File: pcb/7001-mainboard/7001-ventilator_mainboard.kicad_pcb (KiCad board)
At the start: 4 copper layers, 65 x 56.5 mm, 91 parts, among them J1 USB_B_Micro, J10 UART, J2 SWD, J3 Conn_01x02_MountingPin, J4 DNI, J5 24VIN, J6 5V out, J7 PREG_PWR, J8 PREG_SIGNALS, J9 Raspberry_Pi_2_3, Q1 IRLML6244TRPbF, U1 MPRLS0001PG0000SA, U10 ABPMAND001PG2A3, U11 MPVZ5010GW6U, U12 MPVZ5010GW6U, U2 TPD2E2U06, U3 LPC11U37FBD48-401_, U4 MCP1825S, U7 AD5410AREZ, U8 MPRLS0001PG0000SA, U9 ABPMAND001PG2A3, Y1 MCSJK-7U-12.00-10-10-80-B-10

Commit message: schematics: ready for review?
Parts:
- removed Q1: IRLML6244TRPbF, Package_TO_SOT_SMD:SOT-23
- removed TP10: valve_2_fet, TestPoint:TestPoint_Pad_D1.0mm
- added C11: 1uF, Capacitor_SMD:C_0805_2012Metric, F.Cu at (74.0, 218.4)
- added C16: 10uF, Capacitor_SMD:C_0805_2012Metric, F.Cu at (77.5, 215.1)
- added C38: 10uF 50V, Capacitor_SMD:C_1206_3216Metric, F.Cu at (35.8, 230.3)
- added C39: 100nF 50V, Capacitor_SMD:C_0805_2012Metric, F.Cu at (81.9, 206.8)
- added C40: 100nF, Capacitor_SMD:C_0805_2012Metric, F.Cu at (44.0, 233.4)
- added C41: 100nF 50V, Capacitor_SMD:C_0805_2012Metric, F.Cu at (39.6, 233.4)
- added C42: 10uF 50V, Capacitor_SMD:C_1206_3216Metric, F.Cu at (47.0, 230.3)
- added C43: 100nF, Capacitor_SMD:C_0805_2012Metric, F.Cu at (35.2, 233.4)
- added C44: 10uF 50V, Capacitor_SMD:C_1206_3216Metric, F.Cu at (69.0, 218.6)
- added C45: 2.2nF 50V, Capacitor_SMD:C_0805_2012Metric, F.Cu at (48.4, 233.4)
- added D2: D_Schottky, Diode_SMD:D_SOD-123F, F.Cu at (72.6, 215.3)
- added J11: I2C, Jitter_Footprints:TerminalBlock_Wurth_WR-TBL_691322110004_1x04_P3.50mm_Horizontal, F.Cu at (36.2, 208.2)
- added J12: FLOW_SENSORS, Jitter_Footprints:TerminalBlock_Wurth_WR-TBL_691322110003_1x03_P3.50mm_Horizontal, F.Cu at (36.2, 219.8)
- added J13: PREG_PWR, Jitter_Footprints:TerminalBlock_Wurth_WR-TBL_691322110002_1x02_P3.50mm_Horizontal, F.Cu at (49.6, 219.8)
- added J14: PREG_PWR, Jitter_Footprints:TerminalBlock_Wurth_WR-TBL_691322110002_1x02_P3.50mm_Horizontal, F.Cu at (63.1, 208.2)
- added R22: 0, Resistor_SMD:R_0805_2012Metric, F.Cu at (39.6, 245.4)
- added R23: 0, Resistor_SMD:R_0805_2012Metric, F.Cu at (44.0, 239.5)
- added R24: DNI, Resistor_SMD:R_0805_2012Metric, F.Cu at (39.6, 242.4)
- added R25: DNI, Resistor_SMD:R_0805_2012Metric, F.Cu at (35.2, 245.4)
- added R26: DNI, Resistor_SMD:R_0805_2012Metric, F.Cu at (39.6, 239.5)
- added R27: 0, Resistor_SMD:R_0805_2012Metric, F.Cu at (35.2, 242.4)
- added R28: 0, Resistor_SMD:R_0805_2012Metric, F.Cu at (35.2, 239.5)
- added R29: 1k5, Resistor_SMD:R_0805_2012Metric, F.Cu at (68.4, 224.7)
- added R30: DNI, Resistor_SMD:R_0805_2012Metric, F.Cu at (72.8, 221.8)
- added R31: 3.3k, Resistor_SMD:R_0805_2012Metric, F.Cu at (81.9, 212.8)
- added R32: 10k, Resistor_SMD:R_0805_2012Metric, F.Cu at (68.4, 227.7)
- added R33: 1k5, Resistor_SMD:R_0805_2012Metric, F.Cu at (78.5, 218.1)
- added R34: 4.7k, Resistor_SMD:R_0805_2012Metric, F.Cu at (72.8, 224.7)
- added R35: 1k5, Resistor_SMD:R_0805_2012Metric, F.Cu at (77.2, 221.4)
- added R36: 4.7k, Resistor_SMD:R_0805_2012Metric, F.Cu at (68.4, 230.6)
- added U13: ITS4142NHUMA1, Package_TO_SOT_SMD:SOT-223, F.Cu at (74.8, 209.5)
- added U14: ITS4142NHUMA1, Package_TO_SOT_SMD:SOT-223, F.Cu at (61.3, 229.4)
- added U6: LM2937IMP-12/NOPB, Package_TO_SOT_SMD:SOT-223-3_TabPin2, F.Cu at (61.3, 221.1)
- C17: value 2.2nF -> 2.2nF 50V
- C18: value 1uF -> 10uF 50V; footprint Capacitor_SMD:C_0805_2012Metric -> Capacitor_SMD:C_1206_3216Metric
- C19: value 2.2nF -> 100nF 50V
- D1: value BZT52C10+ -> D_Schottky; footprint Diode_SMD:D_SOD-123 -> Diode_SMD:D_SOD-123F
- J3: value Conn_01x02_MountingPin -> 12V; footprint Jitter_Footprints:JST_ZH_S2B-ZR-SM4A-TF_1x02-1MP_P1.5mm_Horizontal -> Jitter_Footprints:TerminalBlock_Wurth_WR-TBL_691322110002_1x02_P3.50mm_Horizontal
- R6: value 1k -> 68k
- R7: value 4.7k -> DNI
- U4: value MCP1825S -> MCP1825S-3302E
- moved C18 213.5 mm to (41.4, 230.3)
- moved R6 211.4 mm to (52.8, 233.4)
- moved D1 207.9 mm to (52.6, 230.3)
- moved R7 190.5 mm to (68.4, 221.8)
- moved J3 188.4 mm to (53.1, 208.2)
- moved C19 170.2 mm to (81.9, 209.8)
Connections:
- C17 pad 1: +6V -> /24V_SW1_OUT
- C18 pad 1: +6V -> +24V
- C19 pad 1: Net-(C19-Pad1) -> +24V
- D1 pad 1: Net-(C19-Pad1) -> /24V_SW1_OUT
- J10 pad 2: /UART_TX -> (no net)
- J10 pad 3: /UART_RX -> (no net)
- J3 pad 1: +6V -> GND
- J3 pad 2: Net-(C19-Pad1) -> +12V
- JP1 pad 1: (no net) -> /DCDC_5V
- R6 pad 2: /pwm_1 -> +24V
- R7 pad 1: GND -> Net-(R30-Pad2)
- R7 pad 2: /pwm_1 -> /DCDC_5V
- U1 pad 12: +3V3 -> Net-(R22-Pad2)
- U10 pad 2: +3V3 -> Net-(R23-Pad2)
- U10 pad 5: /I2C_SCL -> /pressure_sensor/P_SDA
- U10 pad 6: /I2C_SDA -> /pressure_sensor/P_SCL
- U3 pad 30: /pwm_1 -> (no net)
- U8 pad 12: +3V3 -> Net-(R23-Pad2)
- U9 pad 2: +3V3 -> Net-(R22-Pad2)
- U9 pad 5: /I2C_SCL -> /pressure_sensor/P_SDA
- U9 pad 6: /I2C_SDA -> /pressure_sensor/P_SCL
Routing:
- net Net-(R23-Pad2): track 0.00 -> 4.48 mm
- net +3V3: track 4.48 -> 0.00 mm

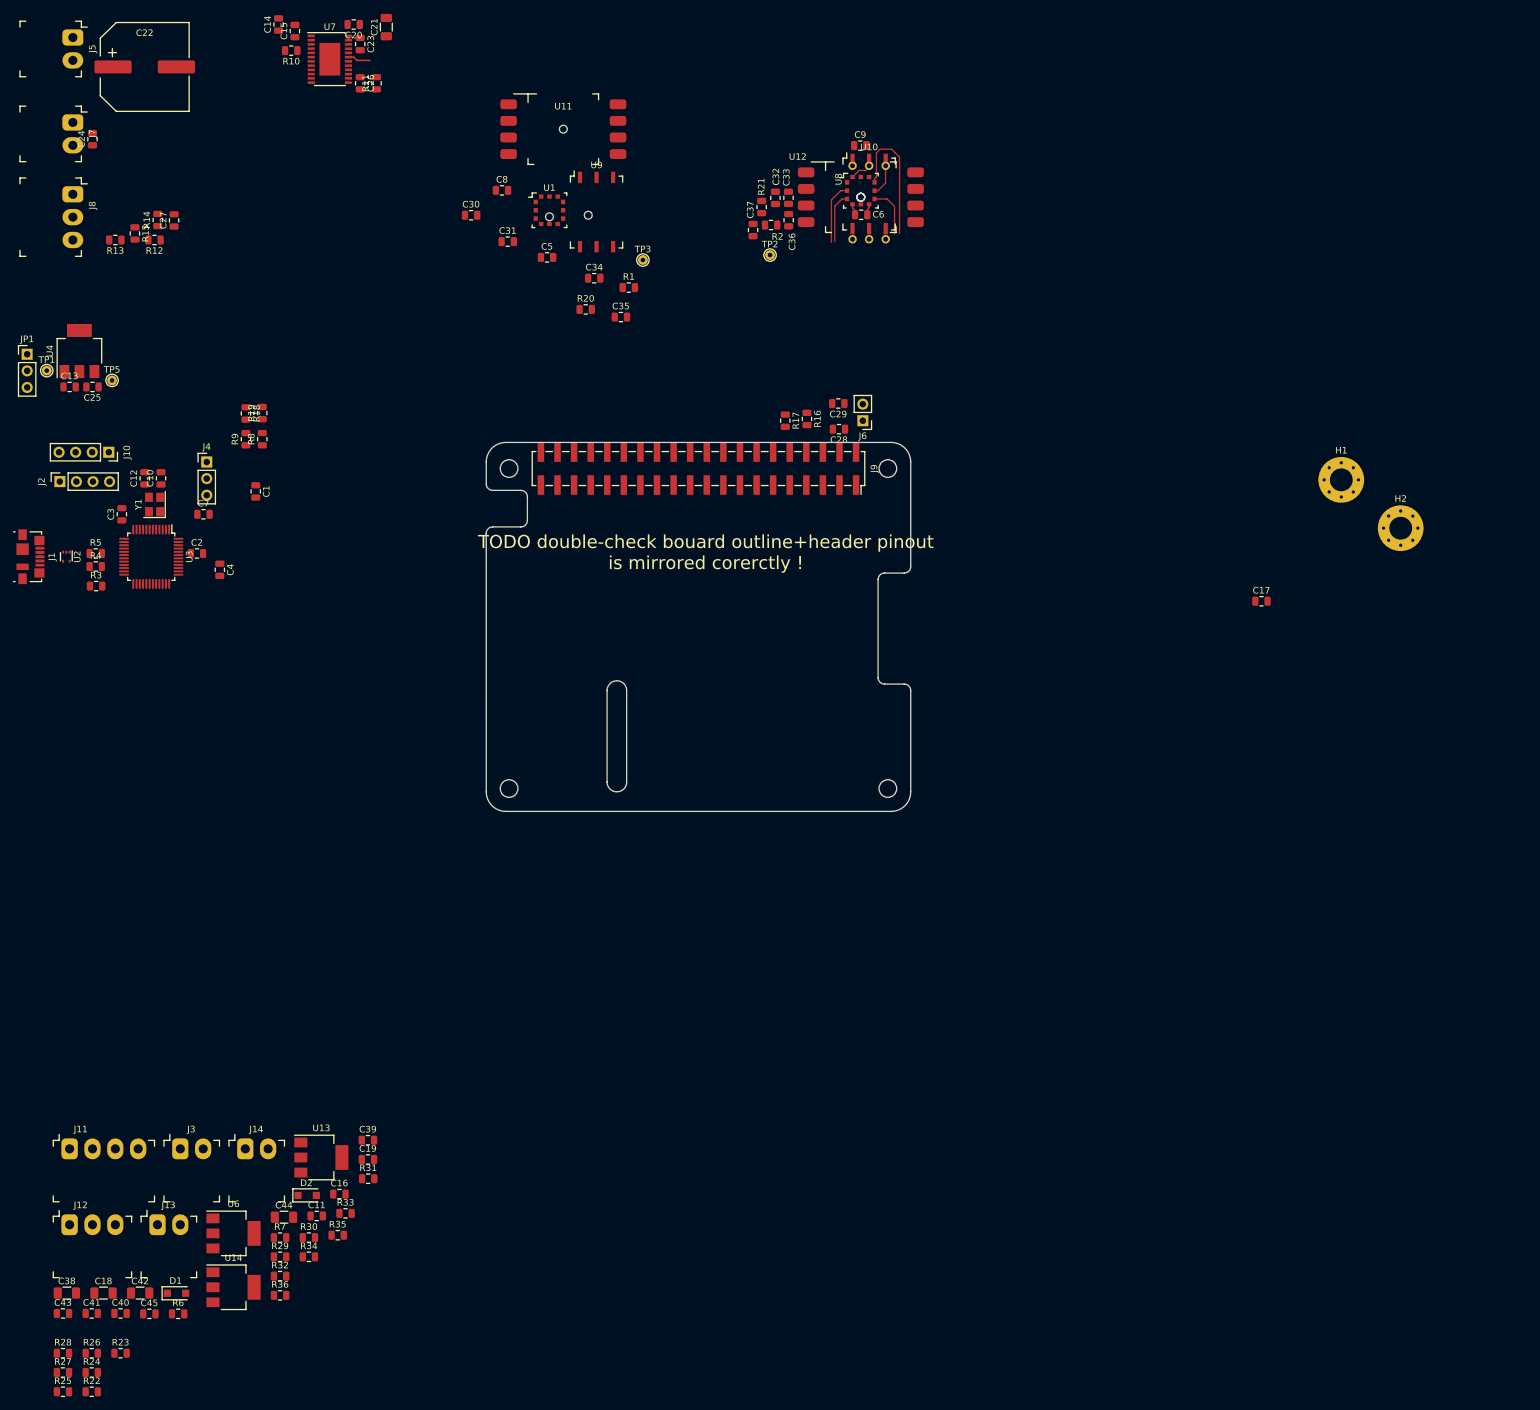
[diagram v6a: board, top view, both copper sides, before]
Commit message: Cleanup BOM, sync with schematic, prepare layout
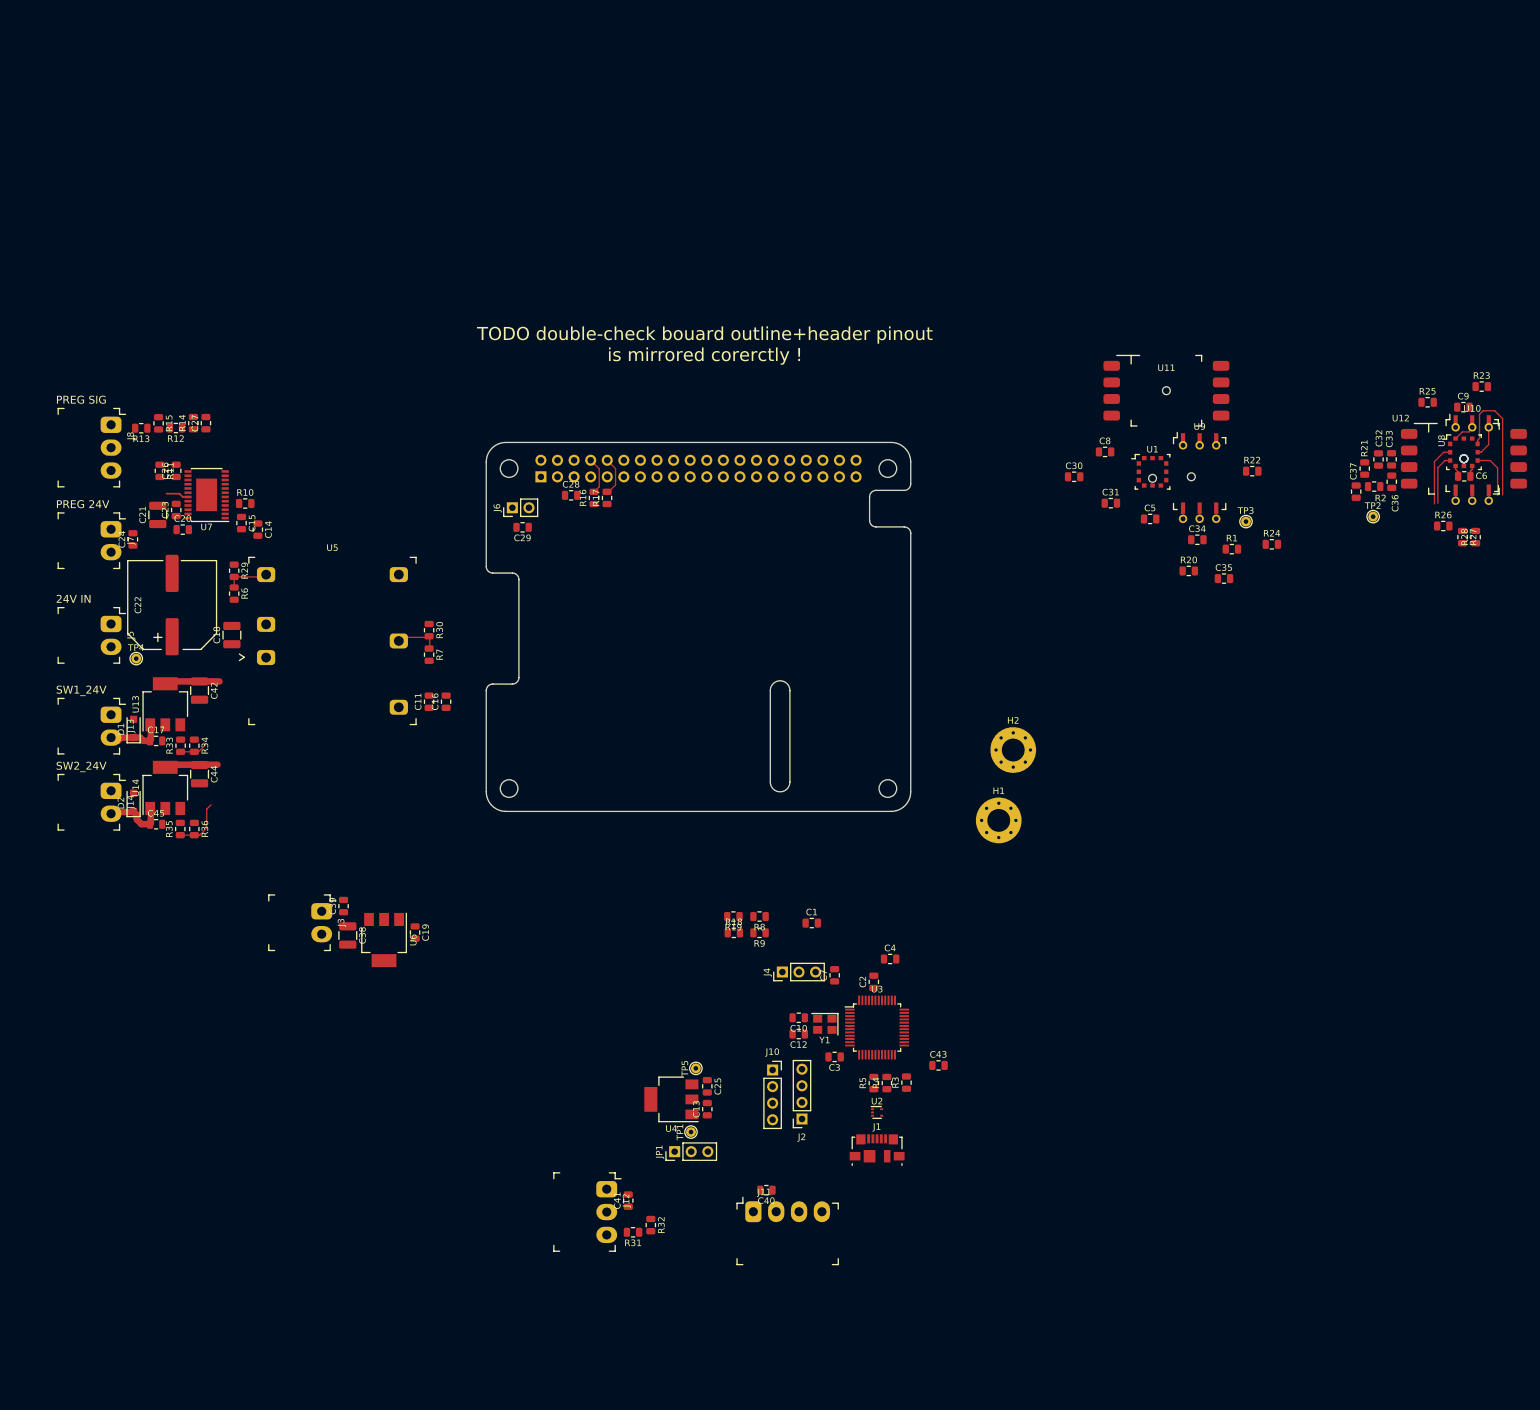
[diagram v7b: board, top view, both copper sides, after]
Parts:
- added TP4: DNI, TestPoint:TestPoint_THTPad_D1.5mm_Drill0.7mm, F.Cu at (46.4, 133.1)
- added U5: S24SE05004PDFA_DC-DC, Jitter_Footprints:DCDC-5V_S24SE05004PDFA, F.Cu at (76.5, 130.4)
- C18, C21, C38, C42, C44: footprint Capacitor_SMD:C_1206_3216Metric -> Capacitor_SMD:C_1210_3225Metric
- H3, H4, H5, H6: moved to F.Cu
- J10: value UART -> 4-pin header
- J11: value I2C -> 4-pin screw terminal
- J12: value FLOW_SENSORS -> 3-pin screw terminal
- J13, J14, J7: value PREG_PWR -> 2-pin screw terminal
- J2: value SWD -> 4-pin header
- J3: value 12V -> 2-pin screw terminal
- J5: value 24VIN -> 2-pin screw terminal
- J8: value PREG_SIGNALS -> 3-pin screw terminal
- J9: footprint Connector_PinSocket_2.54mm:PinSocket_2x20_P2.54mm_Vertical_SMD -> Connector_PinSocket_2.54mm:PinSocket_2x20_P2.54mm_Vertical; moved to B.Cu
- TP1, TP5: value 5V -> DNI
- TP2, TP3: value TestPoint -> DNI
- U9: footprint Jitter_Footprints:ABPMXXX000XX0XX -> Jitter_Footprints:ABPM+DXXX000XX0XX
- Y1: value MCSJK-7U-12.00-10-10-80-B-10 -> 12MHz
- moved R25 258.1 mm to (244.2, 93.8)
- moved R23 255.6 mm to (252.4, 91.5)
- moved R28 249.8 mm to (251.5, 114.5), turned to 90 degrees
- moved R27 249.6 mm to (249.5, 114.5), turned to 270 degrees
- moved R26 242.6 mm to (246.6, 112.8)
- moved R22 226.8 mm to (217.3, 104.4)
- moved R24 220.8 mm to (220.3, 115.6)
- moved C17 170.6 mm to (49.5, 145.7)
- moved J1 158.2 mm to (159.8, 208.1), turned to 0 degrees
- moved JP1 157.3 mm to (128.8, 208.6), turned to 90 degrees
- moved TP1 152.7 mm to (131.3, 205.6), turned to 90 degrees
- moved U2 150.5 mm to (159.8, 202.6), turned to 0 degrees
- moved J2 149.8 mm to (148.3, 203.6), turned to 180 degrees
- moved C13 147.5 mm to (133.8, 202.1), turned to 90 degrees
- moved U4 146.1 mm to (128.3, 200.6), turned to 180 degrees
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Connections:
- J11 pad 2: /I2C_SDA -> +5V
- J11 pad 3: /I2C_SCL -> /I2C_SDA
- J11 pad 4: +5V -> /I2C_SCL
- J12 pad 2: Net-(J12-Pad2) -> +12V
- J12 pad 3: +12V -> Net-(J12-Pad3)
- J8 pad 2: /I_PREG_SETPOINT -> /I_PREG_FEEDBACK
- J8 pad 3: /I_PREG_FEEDBACK -> /I_PREG_SETPOINT
- R31 pad 2: Net-(J12-Pad2) -> Net-(J12-Pad3)
- U3 pad 30: (no net) -> /switch_1_out
- U3 pad 37: (no net) -> /switch_2_out
- U9 pad 4: (no net) -> Net-(U9-Pad4)
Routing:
- net +24V: track 0.00 -> 17.1 mm
- net /24V_SW2_OUT: track 0.00 -> 9.59 mm
- net /24V_SW1_OUT: track 0.00 -> 8.69 mm
- net /switch_2_out: track 0.00 -> 8.32 mm
- net Net-(R30-Pad2): track 0.00 -> 6.77 mm
- net Net-(R29-Pad2): track 0.00 -> 6.70 mm
- net /RPI_RX: track 0.00 -> 6.01 mm
- net /RPI_TX: track 0.00 -> 5.70 mm
- net /switch_1_out: track 0.00 -> 4.45 mm
- net /I_PREG_SETPOINT: track 3.51 -> 4.61 mm
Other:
- outline, holes or cut-outs redrawn
- copper layers 4 -> 2
- board text added: "24V IN"
- board text added: "PREG 24V"
- board text added: "PREG SIG"
- board text added: "SW1_24V"
- board text added: "SW2_24V"
